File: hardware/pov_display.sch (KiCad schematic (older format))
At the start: 36 parts, among them J1 Conn_01x01_Male, J2 Conn_01x01_Male, J3 Conn_01x01_Male, J4 Conn_01x01_Male, J5 Conn_01x01_Male, J6 Conn_01x06_Male, U1 PIC16F676-IP, U2 LM7805_TO220

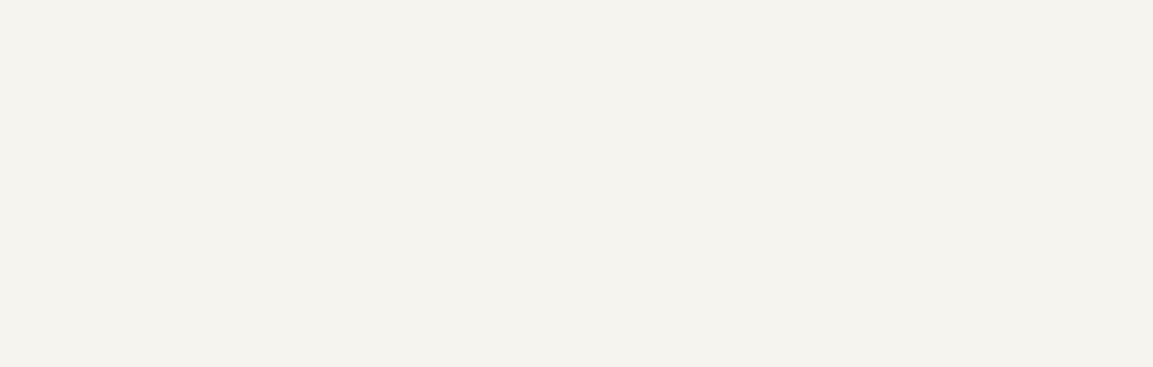
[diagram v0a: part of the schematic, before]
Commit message: Cosmetic updates, removed unwanted files
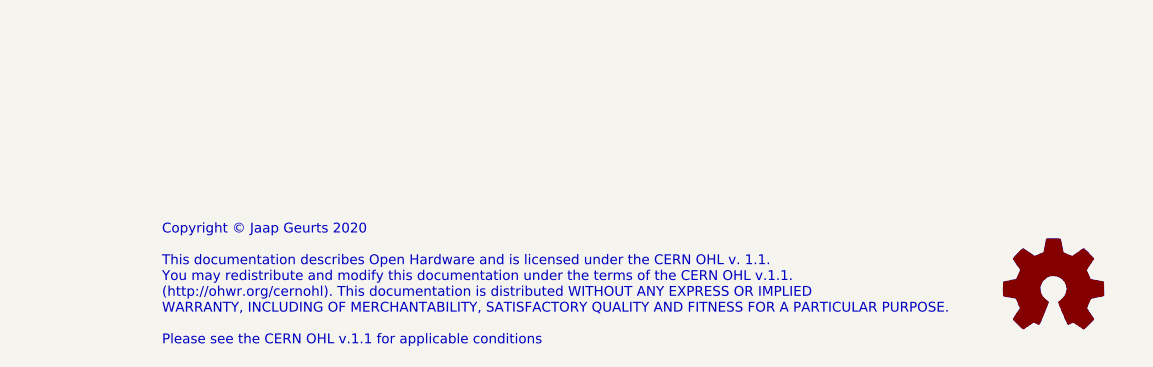
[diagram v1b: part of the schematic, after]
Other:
- note added: "Copyright © Jaap Geurts 2020\n\nThis documentation describes Open Hardware and is licensed under the CERN OHL v. 1.1.\nYou may redistribute and modify this documentation under the terms of the CERN OHL v.1.1.\n(http://ohwr.org/cernohl). This documentation is distributed WITHOUT ANY EXPRESS OR IMPLIED\nWARRANTY, INCLUDING OF MERCHANTABILITY, SATISFACTORY QUALITY AND FITNESS FOR A PARTICULAR PURPOS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"
